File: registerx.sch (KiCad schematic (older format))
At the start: 6 parts, among them U11 74LS245, U12 74LS173, U13 74LS173, U14 74LS245, U15 74LS173, U16 74LS173

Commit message: Added X register
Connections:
- net labels added: ~XI, ~XO
- net labels removed: A0, A1, A10, A11, A12, A13, A14, A15, A2, A3, A4, A5, A6, A7, A8, A9, ~AI, ~AO
- wire segments 234 -> 203

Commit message: Let there be light
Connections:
- wire segments 203 -> 237
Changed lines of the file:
@@
 $Descr A3 16535 11693
 encoding utf-8
-Sheet 11 11
+Sheet 18 20
 Title ""
 Date ""
@@
 	6400 6500 7900 6500
 Wire Wire Line
-	2700 4100 5350 4100
-Wire Wire Line
-	2600 4150 5450 4150
-Wire Wire Line
-	2400 4250 5650 4250
-Wire Wire Line
-	2500 4200 5550 4200
+	2700 4100 4900 4100
+Wire Wire Line
+	2600 4150 4850 4150
+Wire Wire Line
+	2400 4250 4750 4250
+Wire Wire Line
+	2500 4200 4800 4200
 Wire Wire Line
 	2000 6100 4100 6100
@@
 Wire Wire Line
 	2300 5700 3800 5700
+$Sheet
+S 600  5850 550  1800
+U 623AC6EB
+F0 "sheet623AC6D9" 50
+F1 "led16.sch" 50
+F2 "I0" I R 1150 6100 50
+F3 "I1" I R 1150 6200 50
+F4 "I2" I R 1150 6300 50
+F5 "I3" I R 1150 6400 50
+F6 "I4" I R 1150 6500 50
+F7 "I5" I R 1150 6600 50
+F8 "I6" I R 1150 6700 50
+F9 "I7" I R 1150 6800 50
+F10 "I8" I R 1150 6900 50
+F11 "I9" I R 1150 7000 50
+F12 "I10" I R 1150 7100 50
+F13 "I11" I R 1150 7200 50
+F14 "I12" I R 1150 7300 50
+F15 "I13" I R 1150 7400 50
+F16 "I14" I R 1150 7500 50
+F17 "I15" I R 1150 7600 50
+$EndSheet
+Wire Wire Line
+	1150 6100 2000 6100
+Connection ~ 2000 6100
+Wire Wire Line
+	2100 6000 2100 6200
+Wire Wire Line
+	2100 6200 1150 6200
+Connection ~ 2100 6000
+Wire Wire Line
+	1150 6300 2200 6300
+Wire Wire Line
+	2200 6300 2200 5850
+Connection ~ 2200 5850
+Wire Wire Line
+	2300 5700 2300 6400
+Wire Wire Line
+	2300 6400 1150 6400
+Connection ~ 2300 5700
+Wire Wire Line
+	1150 6500 4750 6500
+Wire Wire Line
+	4750 6500 4750 4250
+Connection ~ 4750 4250
+Wire Wire Line
+	4750 4250 5650 4250
+Wire Wire Line
+	1150 6600 4800 6600
+Wire Wire Line
+	4800 6600 4800 4200
+Connection ~ 4800 4200
+Wire Wire Line
+	4800 4200 5550 4200
+Wire Wire Line
+	1150 6700 4850 6700
+Wire Wire Line
+	4850 6700 4850 4150
+Connection ~ 4850 4150
+Wire Wire Line
+	4850 4150 5450 4150
+Wire Wire Line
+	1150 6800 4900 6800
+Wire Wire Line
+	4900 6800 4900 4100
+Connection ~ 4900 4100
+Wire Wire Line
+	4900 4100 5350 4100
+Wire Wire Line
+	1150 6900 6100 6900
+Connection ~ 6100 6900
+Wire Wire Line
+	6200 6800 6200 7000
+Wire Wire Line
+	6200 7000 1150 7000
+Connection ~ 6200 6800
+Wire Wire Line
+	1150 7100 6300 7100
+Wire Wire Line
+	6300 7100 6300 6650
+Connection ~ 6300 6650
+Wire Wire Line
+	1150 7200 6400 7200
+Wire Wire Line
+	6400 7200 6400 6500
+Connection ~ 6400 6500
+Wire Wire Line
+	1150 7300 9750 7300
+Wire Wire Line
+	9750 7300 9750 5050
+Connection ~ 9750 5050
+Wire Wire Line
+	9650 5000 9650 7400
+Wire Wire Line
+	9650 7400 1150 7400
+Connection ~ 9650 5000
+Wire Wire Line
+	1150 7500 9550 7500
+Wire Wire Line
+	9550 7500 9550 4950
+Connection ~ 9550 4950
+Wire Wire Line
+	9450 4900 9450 7600
+Wire Wire Line
+	9450 7600 1150 7600
+Connection ~ 9450 4900
 $EndSCHEMATC

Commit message: Added NAND GATES in ALU
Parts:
- renumbered U11 to U30, U12 to U31, U13 to U32, U14 to U33, U15 to U34, U16 to U35

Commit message: using new RAM and ROM,15bits baby
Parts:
- renumbered U30 to U33, U31 to U34, U32 to U35, U33 to U36, U34 to U37, U35 to U38

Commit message: using new ROM in CU and more jumps
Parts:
- renumbered U33 to U32, U34 to U33, U35 to U34, U36 to U35, U37 to U36, U38 to U37
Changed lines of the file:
@@
 AR Path="/5F74778C/6249200F" Ref="U?"  Part="1"
 AR Path="/5FB94562/6249200F" Ref="U?"  Part="1"
-AR Path="/61DF6CC7/6249200F" Ref="U34"  Part="1"
-F 0 "U34" H 3500 5931 50  0000 C CNN
+AR Path="/61DF6CC7/6249200F" Ref="U33"  Part="1"
+F 0 "U33" H 3500 5931 50  0000 C CNN
 F 1 "74LS173" H 3500 5840 50  0000 C CNN
 F 2 "Package_DIP:DIP-16_W7.62mm" H 3500 4850 50  0001 C CNN
@@
 AR Path="/5F74778C/62492010" Ref="U?"  Part="1"
 AR Path="/5FB94562/62492010" Ref="U?"  Part="1"
-AR Path="/61DF6CC7/62492010" Ref="U33"  Part="1"
-F 0 "U33" V 2546 2656 50  0000 R CNN
+AR Path="/61DF6CC7/62492010" Ref="U32"  Part="1"
+F 0 "U32" V 2546 2656 50  0000 R CNN
 F 1 "74LS245" V 2455 2656 50  0000 R CNN
 F 2 "Package_DIP:DIP-20_W7.62mm" H 2500 3500 50  0001 C CNN
@@
 AR Path="/5F74778C/6249201F" Ref="U?"  Part="1"
 AR Path="/5FB94562/6249201F" Ref="U?"  Part="1"
-AR Path="/61DF6CC7/6249201F" Ref="U38"  Part="1"
-F 0 "U38" V 9104 5244 50  0000 L CNN
+AR Path="/61DF6CC7/6249201F" Ref="U37"  Part="1"
+F 0 "U37" V 9104 5244 50  0000 L CNN
 F 1 "74LS173" V 9195 5244 50  0000 L CNN
 F 2 "Package_DIP:DIP-16_W7.62mm" H 9150 4300 50  0001 C CNN
@@
 AR Path="/5F74778C/5F6AABCF" Ref="U?"  Part="1"
 AR Path="/5FB94562/5F6AABCF" Ref="U?"  Part="1"
-AR Path="/61DF6CC7/5F6AABCF" Ref="U37"  Part="1"
-F 0 "U37" V 7554 6594 50  0000 L CNN
+AR Path="/61DF6CC7/5F6AABCF" Ref="U36"  Part="1"
+F 0 "U36" V 7554 6594 50  0000 L CNN
 F 1 "74LS173" V 7645 6594 50  0000 L CNN
 F 2 "Package_DIP:DIP-16_W7.62mm" H 7600 5650 50  0001 C CNN
@@
 AR Path="/5F74778C/6249201E" Ref="U?"  Part="1"
 AR Path="/5FB94562/6249201E" Ref="U?"  Part="1"
-AR Path="/61DF6CC7/6249201E" Ref="U35"  Part="1"
-F 0 "U35" V 5004 4444 50  0000 L CNN
+AR Path="/61DF6CC7/6249201E" Ref="U34"  Part="1"
+F 0 "U34" V 5004 4444 50  0000 L CNN
 F 1 "74LS173" V 5095 4444 50  0000 L CNN
 F 2 "Package_DIP:DIP-16_W7.62mm" H 5050 3500 50  0001 C CNN
@@
 AR Path="/5F74778C/5F7355A0" Ref="U?"  Part="1"
 AR Path="/5FB94562/5F7355A0" Ref="U?"  Part="1"
-AR Path="/61DF6CC7/5F7355A0" Ref="U36"  Part="1"
-F 0 "U36" V 6646 3456 50  0000 R CNN
+AR Path="/61DF6CC7/5F7355A0" Ref="U35"  Part="1"
+F 0 "U35" V 6646 3456 50  0000 R CNN
 F 1 "74LS245" V 6555 3456 50  0000 R CNN
 F 2 "Package_DIP:DIP-20_W7.62mm" H 6600 4300 50  0001 C CNN

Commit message: fixed more errors
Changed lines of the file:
@@
 	2000 4000 2000 6100
 Wire Wire Line
-	4100 6100 4100 5350
-Wire Wire Line
-	4000 5350 4000 6000
-Wire Wire Line
 	2100 6000 2100 4000
 Wire Wire Line
 	2200 4000 2200 5850
-Wire Wire Line
-	3900 5850 3900 5350
-Wire Wire Line
-	3800 5350 3800 5700
 Wire Wire Line
 	2300 5700 2300 4000
@@
 F 3 "" H 4150 3500 50  0001 C CNN
 	1    4150 3500
-	1    0    0    -1
-$EndComp
-$Comp
-L 16bitCpu-rescue:+5V-power #PWR?
-U 1 1 62492024
-P 4400 4850
-AR Path="/62492024" Ref="#PWR?"  Part="1"
-AR Path="/5F67C726/62492024" Ref="#PWR?"  Part="1"
-AR Path="/5F70885A/62492024" Ref="#PWR?"  Part="1"
-AR Path="/5F733C5E/62492024" Ref="#PWR?"  Part="1"
-AR Path="/602D4838/62492024" Ref="#PWR?"  Part="1"
-AR Path="/603B00C8/62492024" Ref="#PWR?"  Part="1"
-AR Path="/603B766D/62492024" Ref="#PWR?"  Part="1"
-AR Path="/5F74778C/62492024" Ref="#PWR?"  Part="1"
-AR Path="/5FB94562/62492024" Ref="#PWR?"  Part="1"
-AR Path="/61DF6CC7/62492024" Ref="#PWR0137"  Part="1"
-F 0 "#PWR0137" H 4400 4700 50  0001 C CNN
-F 1 "+5V" H 4415 5023 50  0000 C CNN
-F 2 "" H 4400 4850 50  0001 C CNN
-F 3 "" H 4400 4850 50  0001 C CNN
-	1    4400 4850
 	1    0    0    -1
 $EndComp
@@
 Wire Wire Line
 	6500 8600 10200 8600
-$Comp
-L 16bitCpu-rescue:74LS173-74xx U?
-U 1 1 6249200F
-P 3500 4850
-AR Path="/6249200F" Ref="U?"  Part="1"
-AR Path="/5F67C726/6249200F" Ref="U?"  Part="1"
-AR Path="/5F70885A/6249200F" Ref="U?"  Part="1"
-AR Path="/5F733C5E/6249200F" Ref="U?"  Part="1"
-AR Path="/602D4838/6249200F" Ref="U?"  Part="1"
-AR Path="/603B00C8/6249200F" Ref="U?"  Part="1"
-AR Path="/603B766D/6249200F" Ref="U?"  Part="1"
-AR Path="/5F74778C/6249200F" Ref="U?"  Part="1"
-AR Path="/5FB94562/6249200F" Ref="U?"  Part="1"
-AR Path="/61DF6CC7/6249200F" Ref="U33"  Part="1"
-F 0 "U33" H 3500 5931 50  0000 C CNN
-F 1 "74LS173" H 3500 5840 50  0000 C CNN
-F 2 "Package_DIP:DIP-16_W7.62mm" H 3500 4850 50  0001 C CNN
-F 3 "http://www.ti.com/lit/gpn/sn74LS173" H 3500 4850 50  0001 C CNN
-	1    3500 4850
-	0    1    1    0
-$EndComp
 $Comp
 L 16bitCpu-rescue:74LS245-74xx U?
@@
 F 3 "" H 1700 3500 50  0001 C CNN
 	1    1700 3500
-	1    0    0    -1
-$EndComp
-$Comp
-L 16bitCpu-rescue:+5V-power #PWR?
-U 1 1 5F6AAC53
-P 4400 4850
-AR Path="/5F6AAC53" Ref="#PWR?"  Part="1"
-AR Path="/5F67C726/5F6AAC53" Ref="#PWR?"  Part="1"
-AR Path="/5F70885A/5F6AAC53" Ref="#PWR?"  Part="1"
-AR Path="/5F733C5E/5F6AAC53" Ref="#PWR?"  Part="1"
-AR Path="/602D4838/5F6AAC53" Ref="#PWR?"  Part="1"
-AR Path="/603B00C8/5F6AAC53" Ref="#PWR?"  Part="1"
-AR Path="/603B766D/5F6AAC53" Ref="#PWR?"  Part="1"
-AR Path="/5F74778C/5F6AAC53" Ref="#PWR?"  Part="1"
-AR Path="/5FB94562/5F6AAC53" Ref="#PWR?"  Part="1"
-AR Path="/61DF6CC7/5F6AAC53" Ref="#PWR0136"  Part="1"
-F 0 "#PWR0136" H 4400 4700 50  0001 C CNN
-F 1 "+5V" H 4415 5023 50  0000 C CNN
-F 2 "" H 4400 4850 50  0001 C CNN
-F 3 "" H 4400 4850 50  0001 C CNN
-	1    4400 4850
 	1    0    0    -1
 $EndComp
@@
 Text HLabel 1300 2250 0    50   3State ~ 0
 Bus14
-Connection ~ 3600 4350
-Connection ~ 4400 4850
-Connection ~ 2600 4850
 Wire Wire Line
 	10250 3050 10250 7750
@@
 	9450 7600 1150 7600
 Connection ~ 9450 4900
+Connection ~ 2600 4850
+Connection ~ 3600 4350
+Wire Wire Line
+	4100 6100 4100 5350
+Wire Wire Line
+	4000 5350 4000 6000
+Wire Wire Line
+	3900 5850 3900 5350
+Wire Wire Line
+	3800 5350 3800 5700
+$Comp
+L 16bitCpu-rescue:74LS173-74xx U?
+U 1 1 6249200F
+P 3500 4850
+AR Path="/6249200F" Ref="U?"  Part="1"
+AR Path="/5F67C726/6249200F" Ref="U?"  Part="1"
+AR Path="/5F70885A/6249200F" Ref="U?"  Part="1"
+AR Path="/5F733C5E/6249200F" Ref="U?"  Part="1"
+AR Path="/602D4838/6249200F" Ref="U?"  Part="1"
+AR Path="/603B00C8/6249200F" Ref="U?"  Part="1"
+AR Path="/603B766D/6249200F" Ref="U?"  Part="1"
+AR Path="/5F74778C/6249200F" Ref="U?"  Part="1"
+AR Path="/5FB94562/6249200F" Ref="U?"  Part="1"
+AR Path="/61DF6CC7/6249200F" Ref="U33"  Part="1"
+F 0 "U33" H 3500 5931 50  0000 C CNN
+F 1 "74LS173" H 3500 5840 50  0000 C CNN
+F 2 "Package_DIP:DIP-16_W7.62mm" H 3500 4850 50  0001 C CNN
+F 3 "http://www.ti.com/lit/gpn/sn74LS173" H 3500 4850 50  0001 C CNN
+	1    3500 4850
+	0    1    1    0
+$EndComp
+$Comp
+L 16bitCpu-rescue:+5V-power #PWR?
+U 1 1 62492024
+P 4400 4850
+AR Path="/62492024" Ref="#PWR?"  Part="1"
+AR Path="/5F67C726/62492024" Ref="#PWR?"  Part="1"
+AR Path="/5F70885A/62492024" Ref="#PWR?"  Part="1"
+AR Path="/5F733C5E/62492024" Ref="#PWR?"  Part="1"
+AR Path="/602D4838/62492024" Ref="#PWR?"  Part="1"
+AR Path="/603B00C8/62492024" Ref="#PWR?"  Part="1"
+AR Path="/603B766D/62492024" Ref="#PWR?"  Part="1"
+AR Path="/5F74778C/62492024" Ref="#PWR?"  Part="1"
+AR Path="/5FB94562/62492024" Ref="#PWR?"  Part="1"
+AR Path="/61DF6CC7/62492024" Ref="#PWR0137"  Part="1"
+F 0 "#PWR0137" H 4400 4700 50  0001 C CNN
+F 1 "+5V" H 4415 5023 50  0000 C CNN
+F 2 "" H 4400 4850 50  0001 C CNN
+F 3 "" H 4400 4850 50  0001 C CNN
+	1    4400 4850
+	1    0    0    -1
+$EndComp
 $EndSCHEMATC

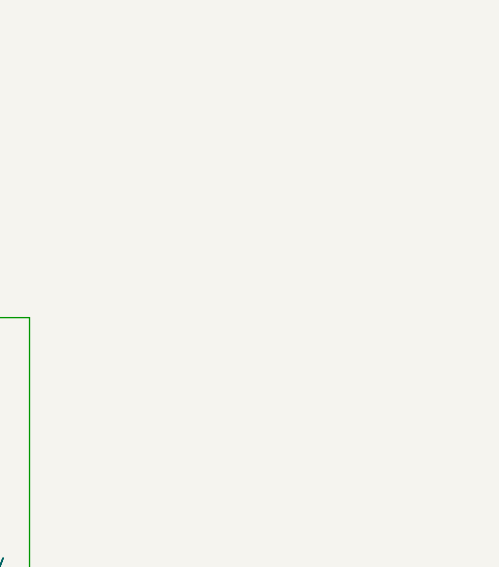
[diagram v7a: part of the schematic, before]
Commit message: added power caps
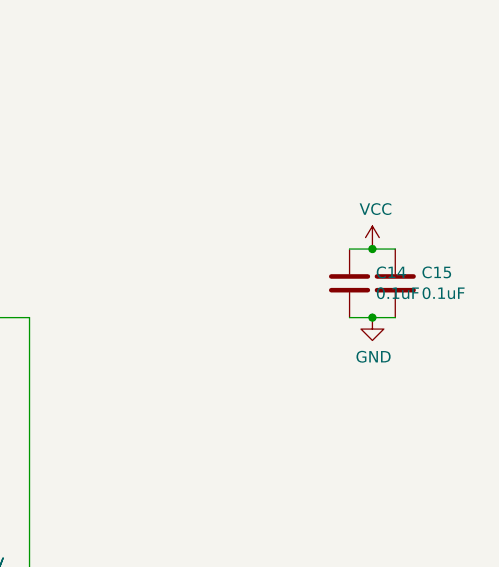
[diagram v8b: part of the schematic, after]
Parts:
- added C14, C15: 0.1uF, Capacitor_THT:CP_Axial_L10.0mm_D4.5mm_P15.00mm_Horizontal, symbol Device:C
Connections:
- net labels added: VCC
- wire segments 237 -> 241
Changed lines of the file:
@@
 $Descr A3 16535 11693
 encoding utf-8
-Sheet 11 21
+Sheet 10 21
 Title ""
 Date ""
@@
 	1    0    0    -1
 $EndComp
+$Comp
+L 16bitCpu-rescue:VCC-power #PWR?
+U 1 1 5FC7F2B9
+P 11750 2750
+AR Path="/5FC7F2B9" Ref="#PWR?"  Part="1"
+AR Path="/61DF6CC7/5FC7F2B9" Ref="#PWR0267"  Part="1"
+F 0 "#PWR0267" H 11750 2600 50  0001 C CNN
+F 1 "VCC" H 11765 2923 50  0000 C CNN
+F 2 "" H 11750 2750 50  0001 C CNN
+F 3 "" H 11750 2750 50  0001 C CNN
+	1    11750 2750
+	1    0    0    -1
+$EndComp
+$Comp
+L 16bitCpu-rescue:GND-power #PWR?
+U 1 1 5FC7F2BF
+P 11750 3050
+AR Path="/5FC7F2BF" Ref="#PWR?"  Part="1"
+AR Path="/5F75E433/5FC7F2BF" Ref="#PWR?"  Part="1"
+AR Path="/61DF6CC7/5FC7F2BF" Ref="#PWR0268"  Part="1"
+F 0 "#PWR0268" H 11750 2800 50  0001 C CNN
+F 1 "GND" H 11755 2877 50  0000 C CNN
+F 2 "" H 11750 3050 50  0001 C CNN
+F 3 "" H 11750 3050 50  0001 C CNN
+	1    11750 3050
+	1    0    0    -1
+$EndComp
+Wire Wire Line
+	11750 2750 11850 2750
+Wire Wire Line
+	11850 3050 11750 3050
+$Comp
+L Device:C C?
+U 1 1 5FC7F2C7
+P 11650 2900
+AR Path="/5F75E433/5FC7F2C7" Ref="C?"  Part="1"
+AR Path="/61DF6CC7/5FC7F2C7" Ref="C14"  Part="1"
+F 0 "C14" H 11765 2946 50  0000 L CNN
+F 1 "0.1uF" H 11765 2855 50  0000 L CNN
+F 2 "Capacitor_THT:CP_Axial_L10.0mm_D4.5mm_P15.00mm_Horizontal" H 11688 2750 50  0001 C CNN
+F 3 "" H 11650 2900 50  0001 C CNN
+	1    11650 2900
+	1    0    0    -1
+$EndComp
+Wire Wire Line
+	11750 2750 11650 2750
+Connection ~ 11750 2750
+Wire Wire Line
+	11650 3050 11750 3050
+Connection ~ 11750 3050
+$Comp
+L Device:C C?
+U 1 1 5FC7F2D1
+P 11850 2900
+AR Path="/5F75E433/5FC7F2D1" Ref="C?"  Part="1"
+AR Path="/61DF6CC7/5FC7F2D1" Ref="C15"  Part="1"
+F 0 "C15" H 11965 2946 50  0000 L CNN
+F 1 "0.1uF" H 11965 2855 50  0000 L CNN
+F 2 "Capacitor_THT:CP_Axial_L10.0mm_D4.5mm_P15.00mm_Horizontal" H 11888 2750 50  0001 C CNN
+F 3 "" H 11850 2900 50  0001 C CNN
+	1    11850 2900
+	1    0    0    -1
+$EndComp
